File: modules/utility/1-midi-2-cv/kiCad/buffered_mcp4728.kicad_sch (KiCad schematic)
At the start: 18 parts, among them U3 MCP4728, U4 TL074

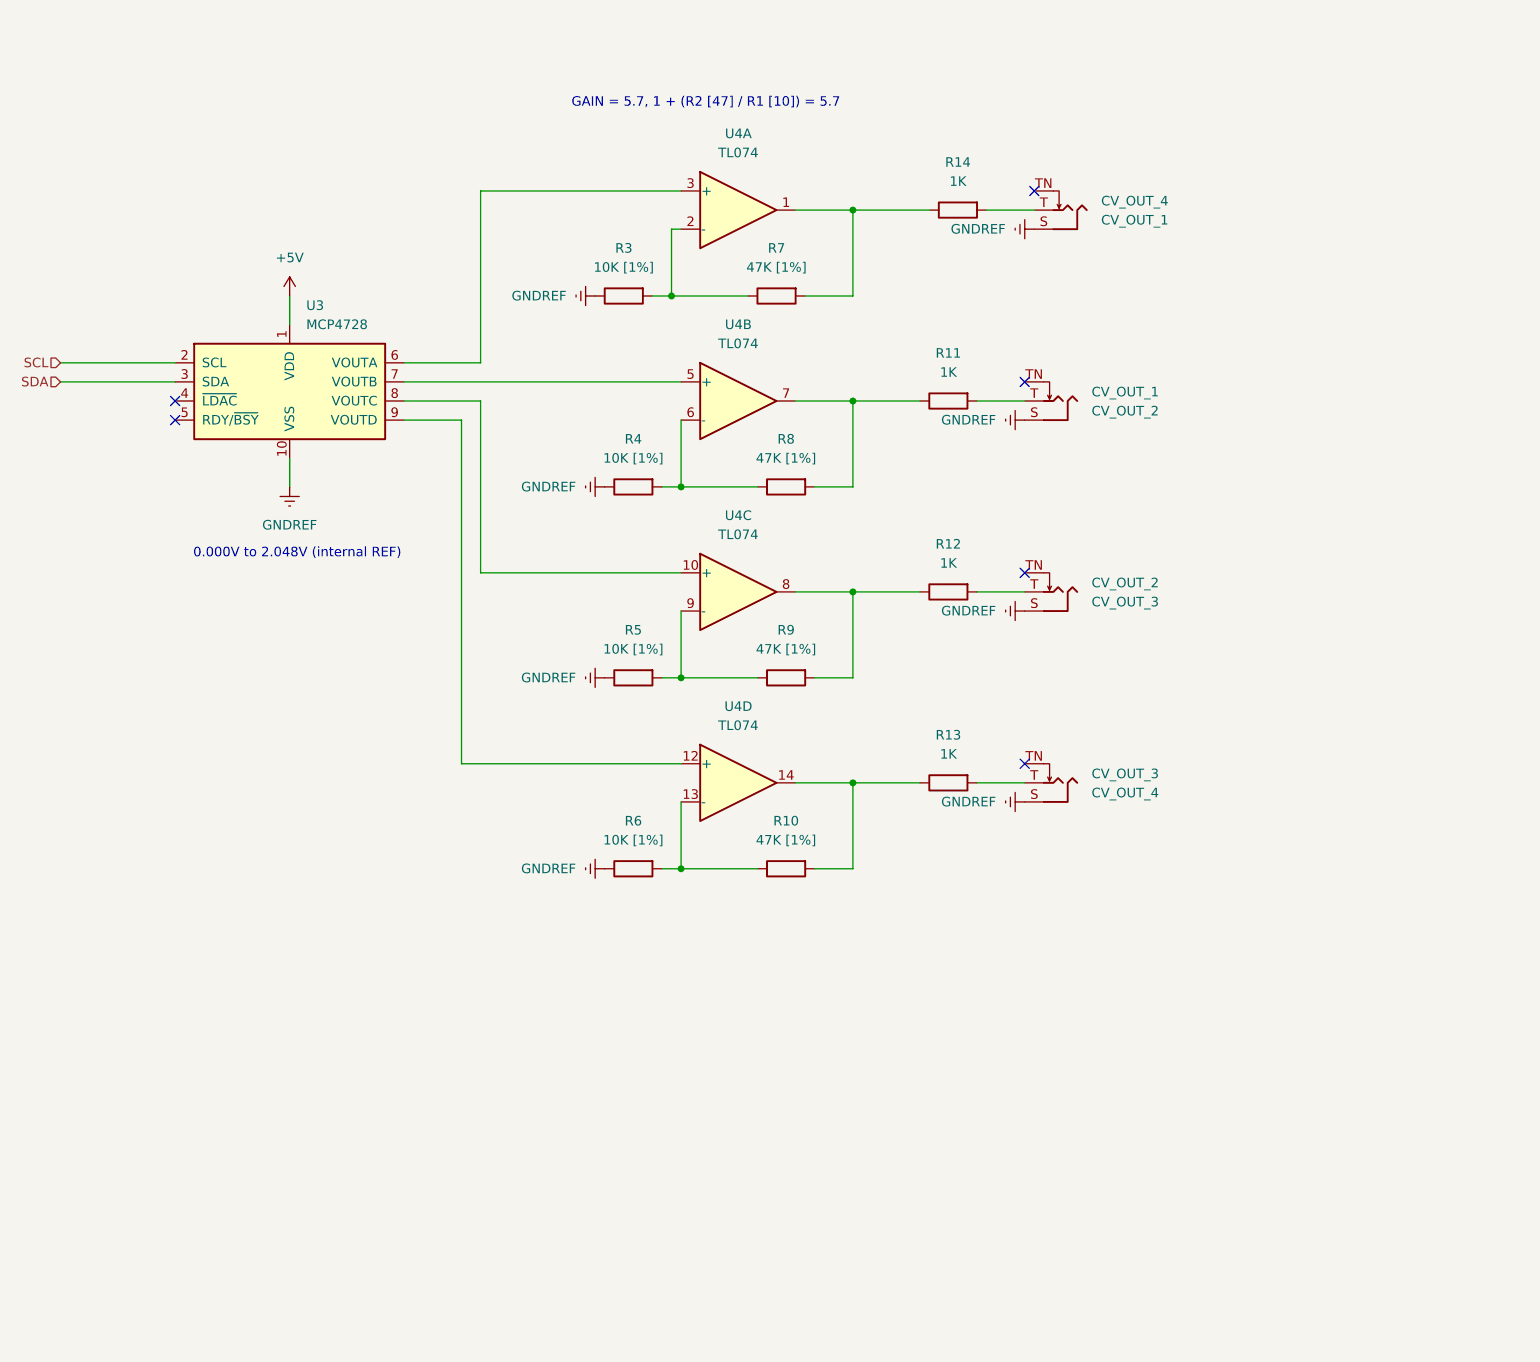
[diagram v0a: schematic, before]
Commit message: dd some more modules, update src for midi-2-cv
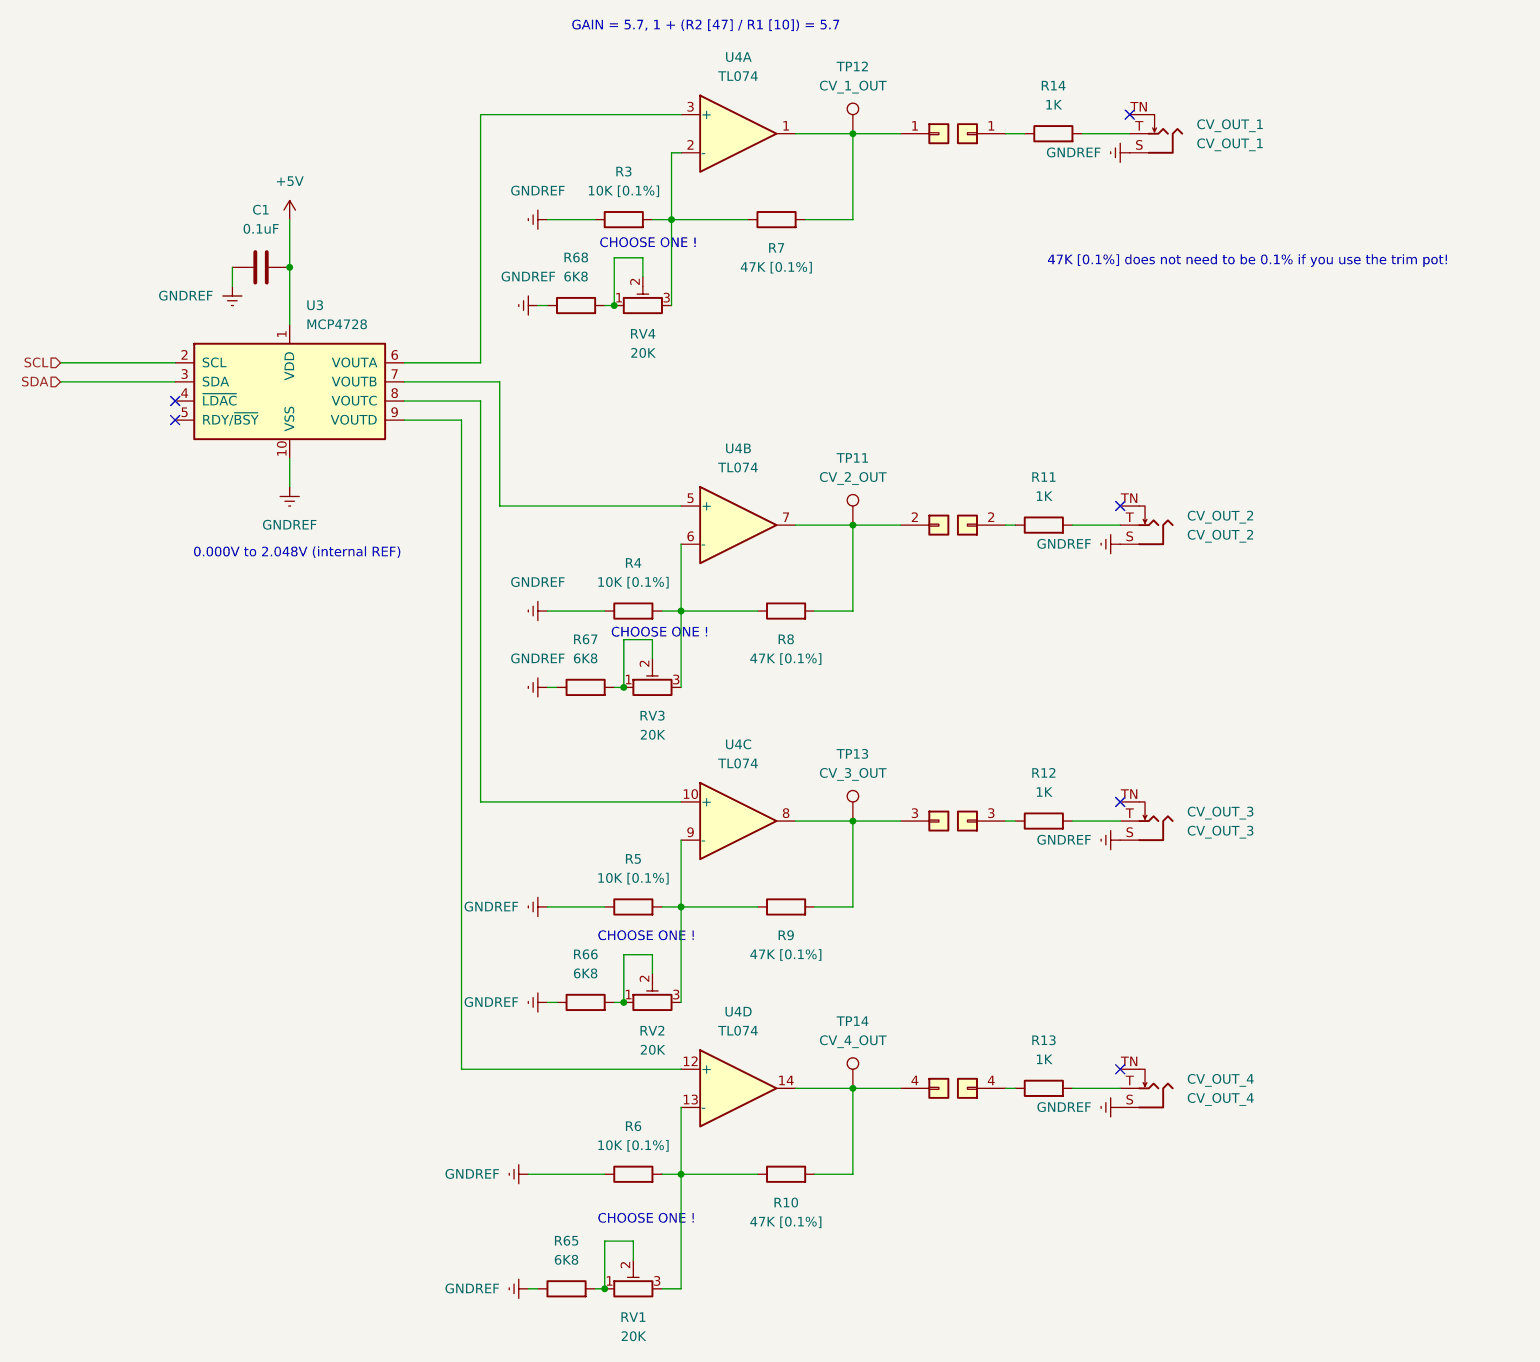
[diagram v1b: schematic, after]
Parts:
- added C1: 0.1uF, Capacitor_SMD:C_0805_2012Metric_Pad1.18x1.45mm_HandSolder, symbol Device:C
- added H3: PinSocket_01x04, Synth:PinSocket_1x04_P2.54mm_Vertical, symbol synth:PinSocket_01x04
- added H4: PinHeader_01x04, Synth:PinHeader_1x04_P2.54mm_Vertical, symbol synth:PinHeader_01x04
- added R65, R66, R67, R68: 6K8, Resistor_SMD:R_0805_2012Metric_Pad1.20x1.40mm_HandSolder, symbol Device:R
- added RV1, RV2, RV3, RV4: 20K, Potentiometer_THT:Potentiometer_Piher_PT-6-V_Vertical, symbol Device:R_Potentiometer_Trim
- added TP11: CV_2_OUT, Connector_Pin:Pin_D1.0mm_L10.0mm, symbol Connector:TestPoint
- added TP12: CV_1_OUT, Connector_Pin:Pin_D1.0mm_L10.0mm, symbol Connector:TestPoint
- added TP13: CV_3_OUT, Connector_Pin:Pin_D1.0mm_L10.0mm, symbol Connector:TestPoint
- added TP14: CV_4_OUT, Connector_Pin:Pin_D1.0mm_L10.0mm, symbol Connector:TestPoint
- R10, R7, R8, R9: value 47K [1%] -> 47K [0.1%]; footprint Synth:R_Default (DIN0207) -> Resistor_SMD:R_0805_2012Metric_Pad1.20x1.40mm_HandSolder; symbol synth:R_Default -> Device:R
- R11, R12, R13, R14: footprint Synth:R_Default (DIN0207) -> Resistor_SMD:R_0805_2012Metric_Pad1.20x1.40mm_HandSolder; symbol synth:R_Default -> Device:R
- R3, R4, R5, R6: value 10K [1%] -> 10K [0.1%]; footprint Synth:R_Default (DIN0207) -> Resistor_SMD:R_0805_2012Metric_Pad1.20x1.40mm_HandSolder; symbol synth:R_Default -> Device:R
- renumbered CV_OUT_4 to CV_OUT_1, CV_OUT_1 to CV_OUT_2, CV_OUT_2 to CV_OUT_3, CV_OUT_3 to CV_OUT_4
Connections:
- net +5V: now also C1.2
- net GNDREF: now also R3.1, R4.1, R5.1, R6.1, C1.1, R65.1, R66.1, R67.1, R68.1; no longer R3.2, R4.2, R5.2, R6.2
- net at CV_OUT_4.T: now also R13.2; no longer R13.1
- net at CV_OUT_3.T: now also R12.2; no longer R12.1
- net at R11.1: now also H4.2 (Pin_2); no longer CV_OUT_2.T
- net at CV_OUT_1.T: now also R14.2; no longer R14.1
- new net: H3.4 (Pin_4), R10.2, TP14.1, U4.14
- new net: R68.2, RV4.1, RV4.2
- new net: R3.2, R7.1, RV4.3, U4.2 (-)
- new net: H3.2 (Pin_2), R8.2, TP11.1, U4.7
- new net: R5.2, R9.1, RV2.3, U4.9 (-)
- new net: H3.3 (Pin_3), R9.2, TP13.1, U4.8
- new net: H4.3 (Pin_3), R12.1
- new net: R10.1, R6.2, RV1.3, U4.13 (-)
- new net: R66.2, RV2.1, RV2.2
- new net: H4.4 (Pin_4), R13.1
- new net: R65.2, RV1.1, RV1.2
- new net: CV_OUT_2.T, R11.2
- new net: R4.2, R8.1, RV3.3, U4.6 (-)
- new net: H3.1 (Pin_1), R7.2, TP12.1, U4.1
- new net: R67.2, RV3.1, RV3.2
- new net: H4.1 (Pin_1), R14.1
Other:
- note added: "47K [0.1%] does not need to be 0.1% if you use the trim pot!"
- note added: "CHOOSE ONE !"
- moved on the sheet: CV_OUT_1, CV_OUT_2, CV_OUT_3, CV_OUT_4, R10, R11, R12, R13, R14, R3, R4, R5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

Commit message: Midi 2 CV (Midas) Rework; Delay (Richochet) Rework. Programming, backups for WeAct CV
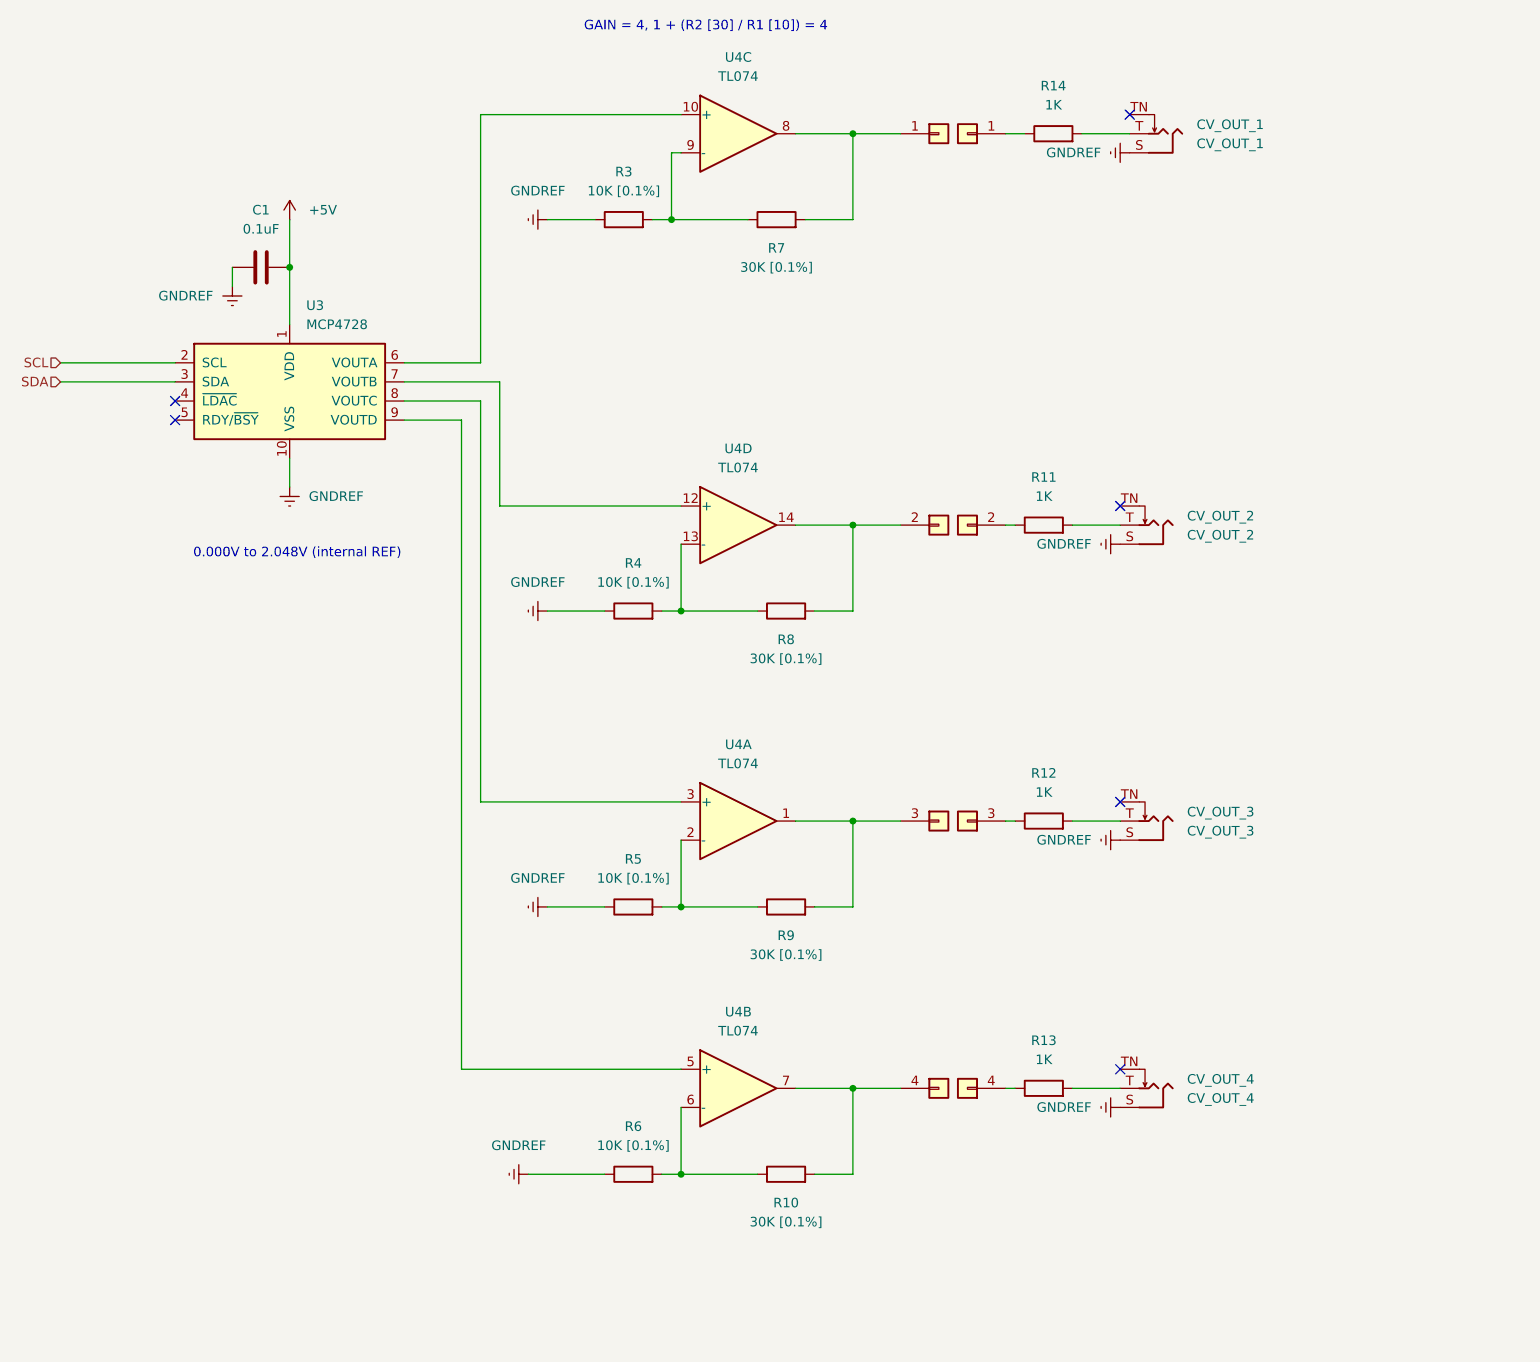
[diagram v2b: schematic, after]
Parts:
- removed R65, R66, R67, R68: 6K8, Resistor_SMD:R_0805_2012Metric_Pad1.20x1.40mm_HandSolder, symbol Device:R
- removed RV1, RV2, RV3, RV4: 20K, Potentiometer_THT:Potentiometer_Piher_PT-6-V_Vertical, symbol Device:R_Potentiometer_Trim
- removed TP11: CV_2_OUT, Connector_Pin:Pin_D1.0mm_L10.0mm, symbol Connector:TestPoint
- removed TP12: CV_1_OUT, Connector_Pin:Pin_D1.0mm_L10.0mm, symbol Connector:TestPoint
- removed TP13: CV_3_OUT, Connector_Pin:Pin_D1.0mm_L10.0mm, symbol Connector:TestPoint
- removed TP14: CV_4_OUT, Connector_Pin:Pin_D1.0mm_L10.0mm, symbol Connector:TestPoint
- R10, R7, R8, R9: value 47K [0.1%] -> 30K [0.1%]
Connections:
- net at H3.4 (Pin_4), R10.2: now also U4.7; no longer U4.14
- net at R3.2, R7.1: now also U4.9 (-); no longer U4.2 (-)
- net at H3.2 (Pin_2), R8.2: now also U4.14; no longer U4.7
- net at R5.2, R9.1: now also U4.2 (-); no longer U4.9 (-)
- net at H3.3 (Pin_3), R9.2: now also U4.1; no longer U4.8
- net at R10.1, R6.2: now also U4.6 (-); no longer U4.13 (-)
- net at U3.6 (VOUTA): now also U4.10 (+); no longer U4.3 (+)
- net at U3.7 (VOUTB): now also U4.12 (+); no longer U4.5 (+)
- net at U3.8 (VOUTC): now also U4.3 (+); no longer U4.10 (+)
- net at U3.9 (VOUTD): now also U4.5 (+); no longer U4.12 (+)
- net at R4.2, R8.1: now also U4.13 (-); no longer U4.6 (-)
- net at H3.1 (Pin_1), R7.2: now also U4.8; no longer U4.1
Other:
- note added: "GAIN = 4, 1 + (R2 [30] / R1 [10]) = 4"
- note removed: "47K [0.1%] does not need to be 0.1% if you use the trim pot!"
- note removed: "CHOOSE ONE !"
- note removed: "GAIN = 5.7, 1 + (R2 [47] / R1 [10]) = 5.7"
- company: (none) -> Lentronics
- title: (none) -> midas_control-voltage
